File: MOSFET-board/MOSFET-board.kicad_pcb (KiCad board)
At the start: 2 copper layers, 88.9 x 76.2 mm, 141 parts, among them J1 PCIE-LP-01-01-F-DV-A-TR, J2 DB15_Female, J3 DB15_Female, U1 BTS3080EJXUMA1, U10 BTS3080EJXUMA1, U11 PCF8575_Breakout, U2 BTS3080EJXUMA1, U22 ADA4897-1ARJZ-R7, U23 ADA4897-1ARJZ-R7, U24 ADA4897-1ARJZ-R7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

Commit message: 16X symbol setup and mosfet schematic
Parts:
- removed J1: PCIE-LP-01-01-F-DV-A-TR, Connector_PCBEdge:BUS_PCIexpress_x1
- added J4: Bus_PCI_Express_x16, Connector_PCBEdge:BUS_PCIexpress_x16, B.Cu at (208.3, 152.4)
- moved F1 0.24 mm to (205.7, 129.5)
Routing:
- net Net-(F1-Pad1): track 43.4 -> 66.1 mm
- net unconnected-(J4-~{PERST}-PadA11): track 0.00 -> 6.54 mm
- net +3.3V: track 6.54 -> 0.00 mm

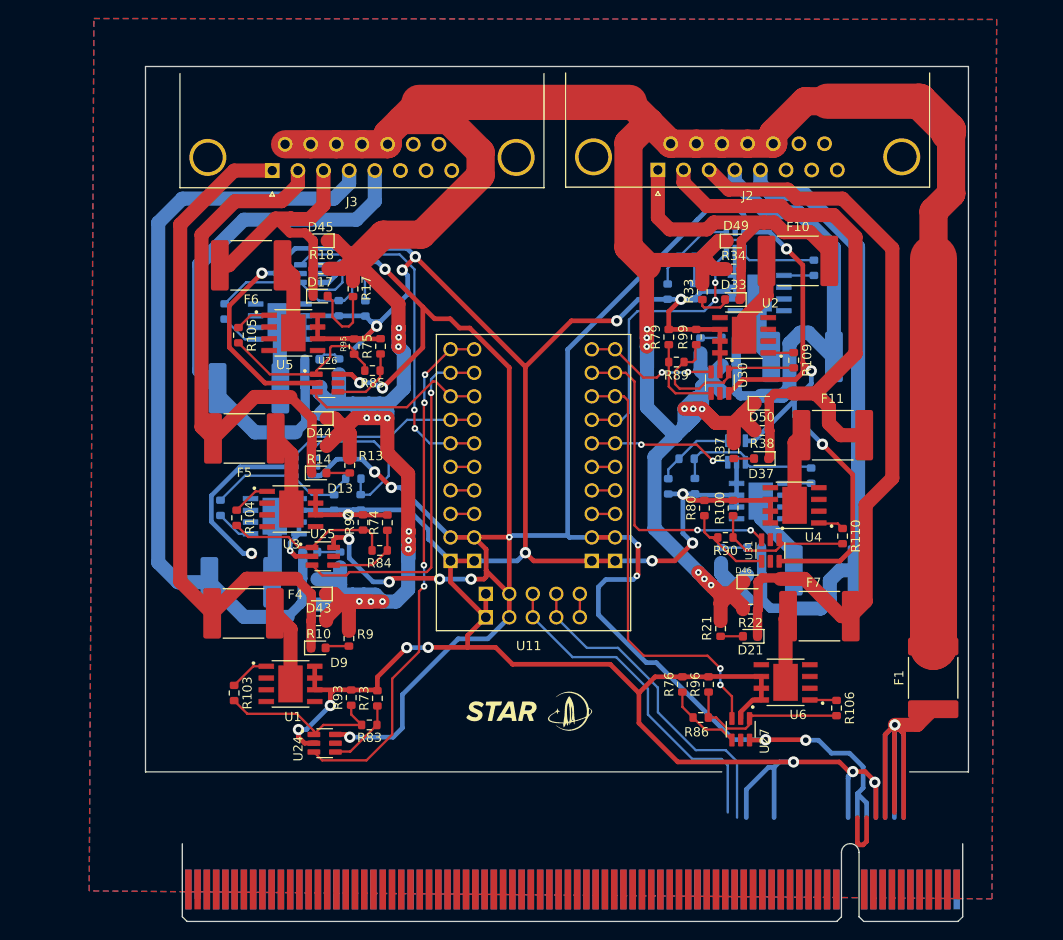
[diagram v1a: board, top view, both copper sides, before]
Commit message: mosfet routing
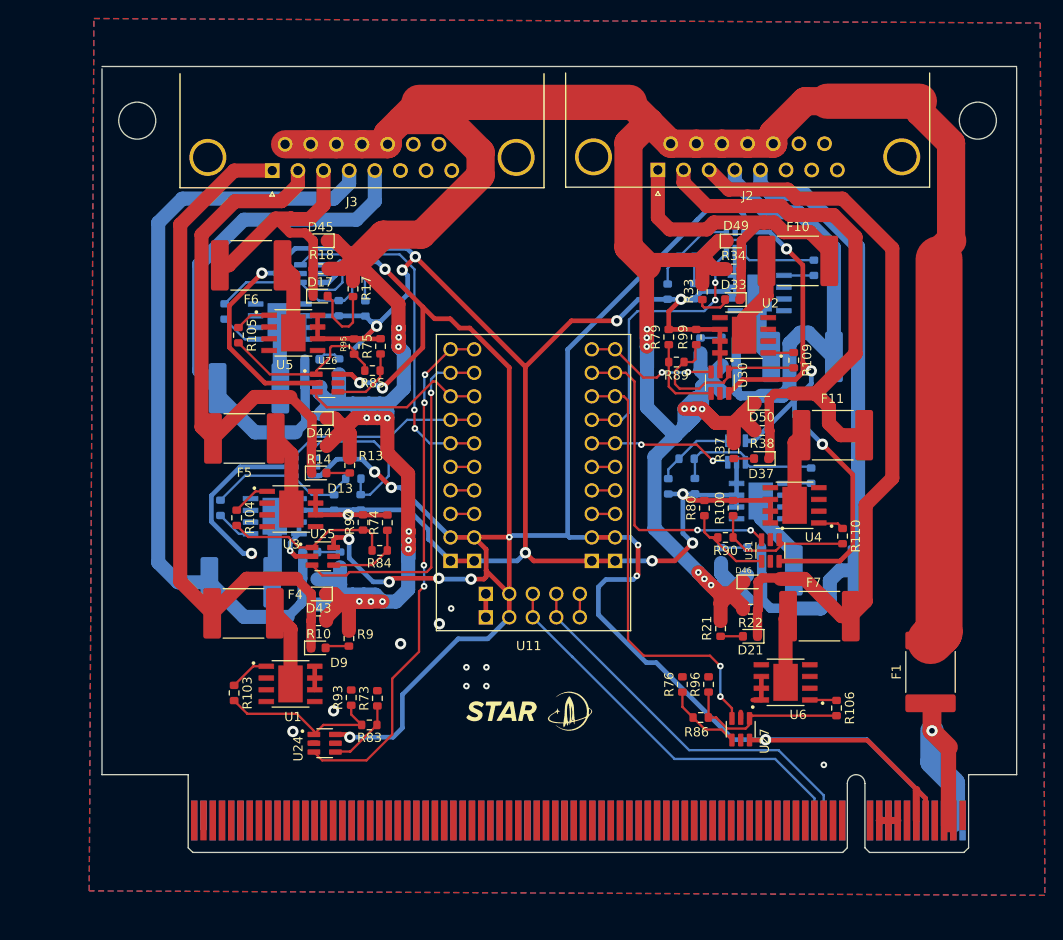
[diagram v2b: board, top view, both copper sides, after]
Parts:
- moved J4 7.48 mm to (208.9, 144.9)
- moved F1 0.70 mm to (205.5, 128.9)
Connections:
- J4 pad A8: unconnected-(J4-JTAG5-PadA8) -> +3.3V
- J4 pad B9: unconnected-(J4-JTAG1-PadB9) -> +3.3V
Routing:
- net GND: track 422.9 -> 287.4 mm, vias 20 -> 23
- net Net-(F1-Pad1): track 66.1 -> 23.9 mm
- net +5V: track 337.1 -> 364.6 mm, vias 18 -> 17
- net I2C_SDA: track 37.0 -> 43.5 mm
- net unconnected-(J4-~{PERST}-PadA11): track 6.54 -> 0.00 mm
- net I2C_SCL: track 36.1 -> 42.1 mm
- net +3.3V: track 0.00 -> 4.00 mm
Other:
- board size 88.9 x 76.2 mm -> 98.8 x 76.5 mm

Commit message: mosfet board updates. GND tracing removals and aux scl/sda
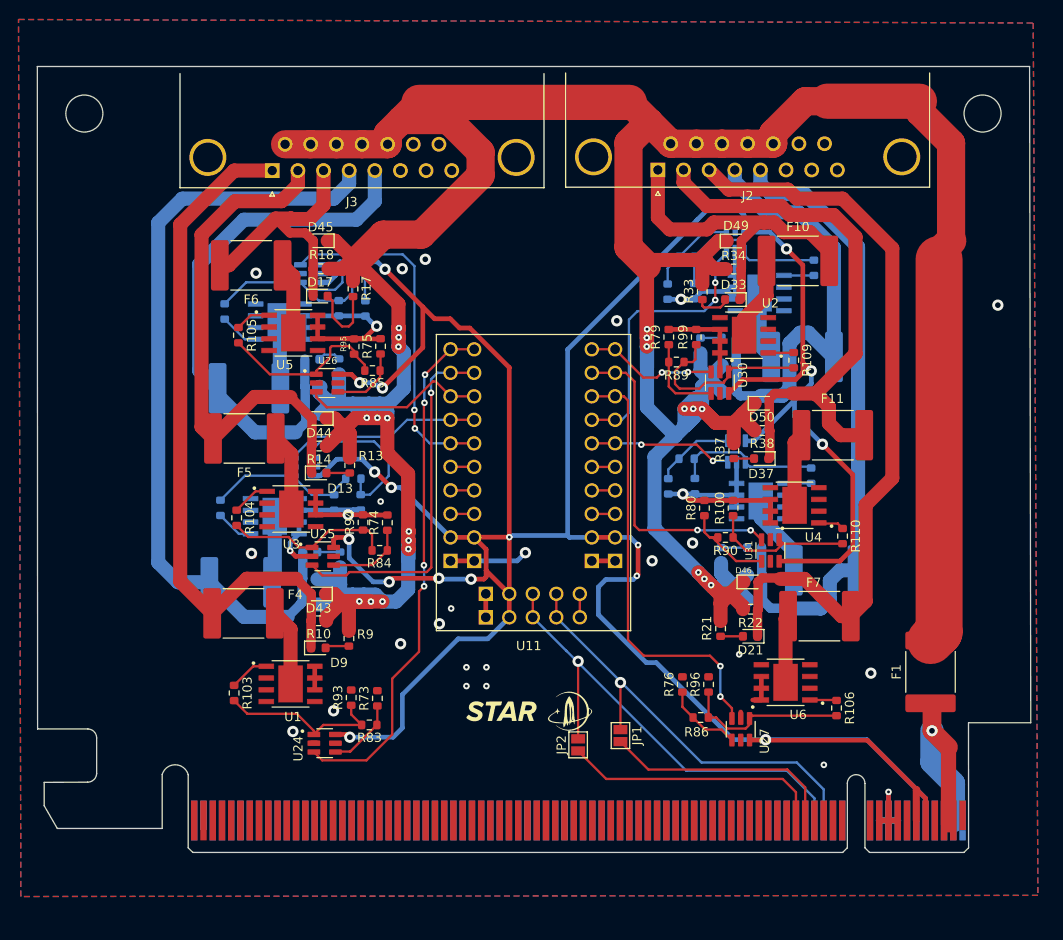
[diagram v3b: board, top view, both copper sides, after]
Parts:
- added JP1: SCL_AUX, Jumper:SolderJumper-2_P1.3mm_Open_Pad1.0x1.5mm, F.Cu at (172.0, 135.8)
- added JP2: SDA_AUX, Jumper:SolderJumper-2_P1.3mm_Open_Pad1.0x1.5mm, F.Cu at (167.4, 136.8)
- J4: footprint Connector_PCBEdge:BUS_PCIexpress_x16 -> PCIe_x16_DAQ:Custom-16x-PCIELock
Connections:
- J4 pad A16: unconnected-(J4-PERp0-PadA16) -> Net-(J4-I2C_SCL_AUX)
- J4 pad A17: unconnected-(J4-PERn0-PadA17) -> Net-(J4-I2C_SDA_AUX)
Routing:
- net GND: track 287.4 -> 119.4 mm, vias 23 -> 27
- net Net-(J4-I2C_SDA_AUX): track 0.00 -> 28.4 mm
- net Net-(J4-I2C_SCL_AUX): track 0.00 -> 25.6 mm
- net I2C_SDA: track 43.5 -> 52.1 mm, vias 0 -> 1
- net +3.3V: track 4.00 -> 10.3 mm, vias 0 -> 1
- net I2C_SCL: track 42.1 -> 47.6 mm, vias 0 -> 1
- net +5V: track 364.6 -> 368.0 mm
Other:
- board size 98.8 x 76.5 mm -> 107.3 x 71.6 mm

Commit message: core, mosfet
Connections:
- J4 pad A1: unconnected-(J4-~{PRSNT1}-PadA1) -> Net-(F1-Pad1)
- J4 pad A7: unconnected-(J4-JTAG4-PadA7) -> GND
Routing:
- net Net-(F1-Pad1): track 23.9 -> 28.6 mm
